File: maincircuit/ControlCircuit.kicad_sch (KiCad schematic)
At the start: 4 parts, among them J1 Conn_01x14_Socket, J2 Conn_01x14_Socket, J3 Conn_01x02_Pin, J4 Conn_01x02_Pin

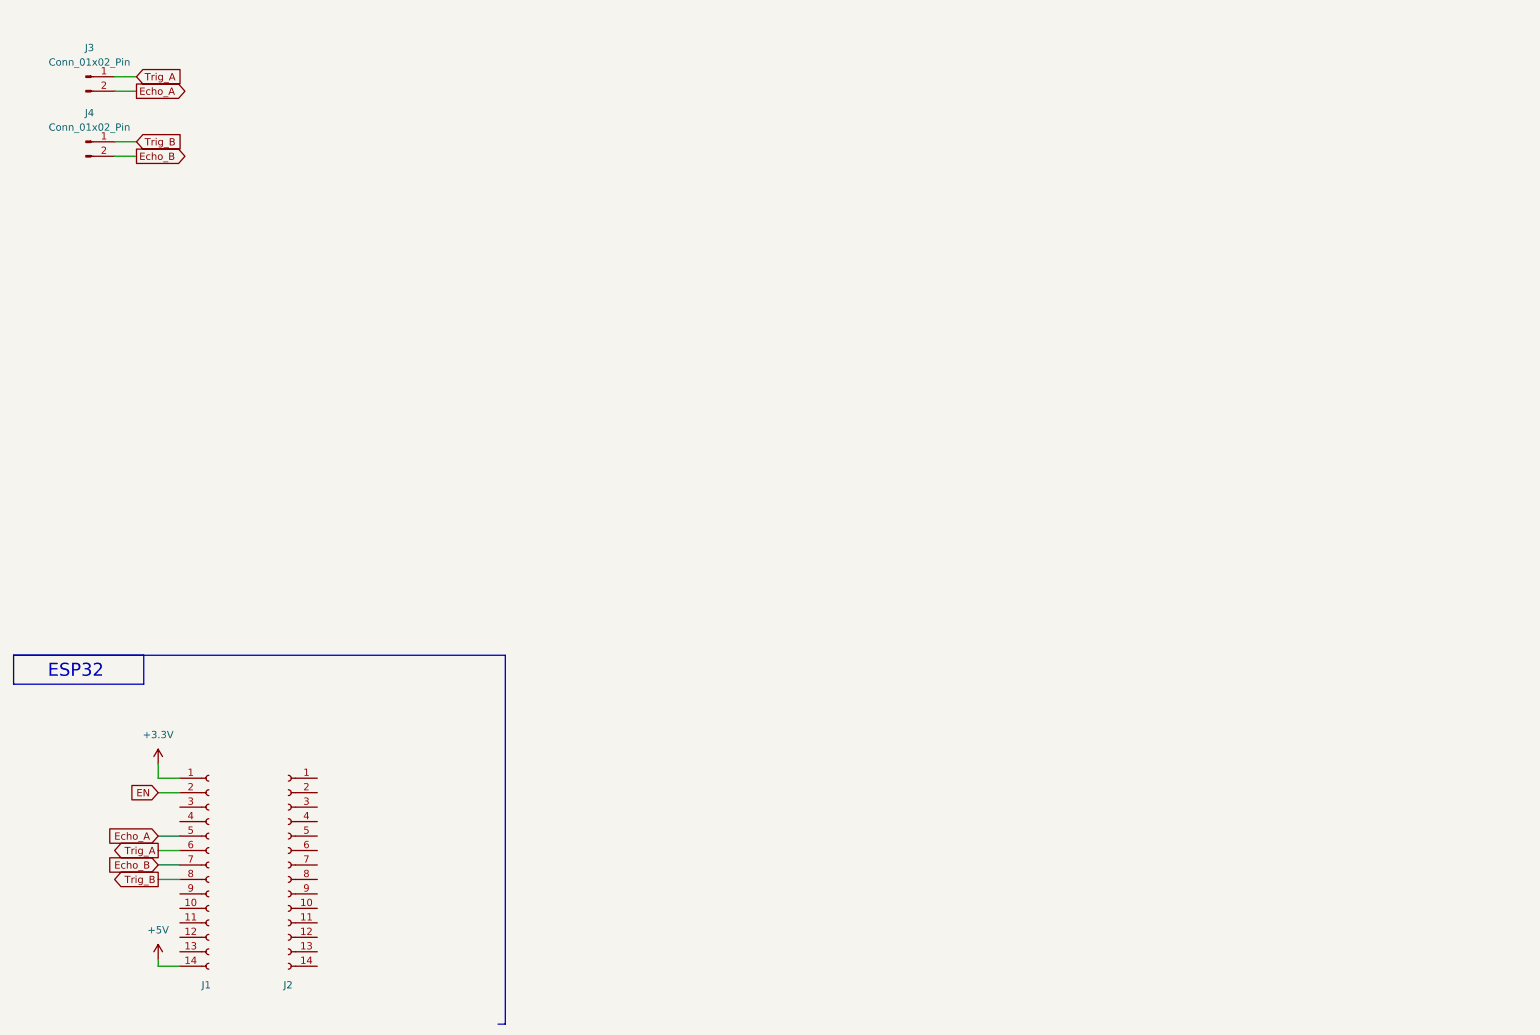
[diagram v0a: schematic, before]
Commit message: add: 07/13進捗分(主にcontrol回路)
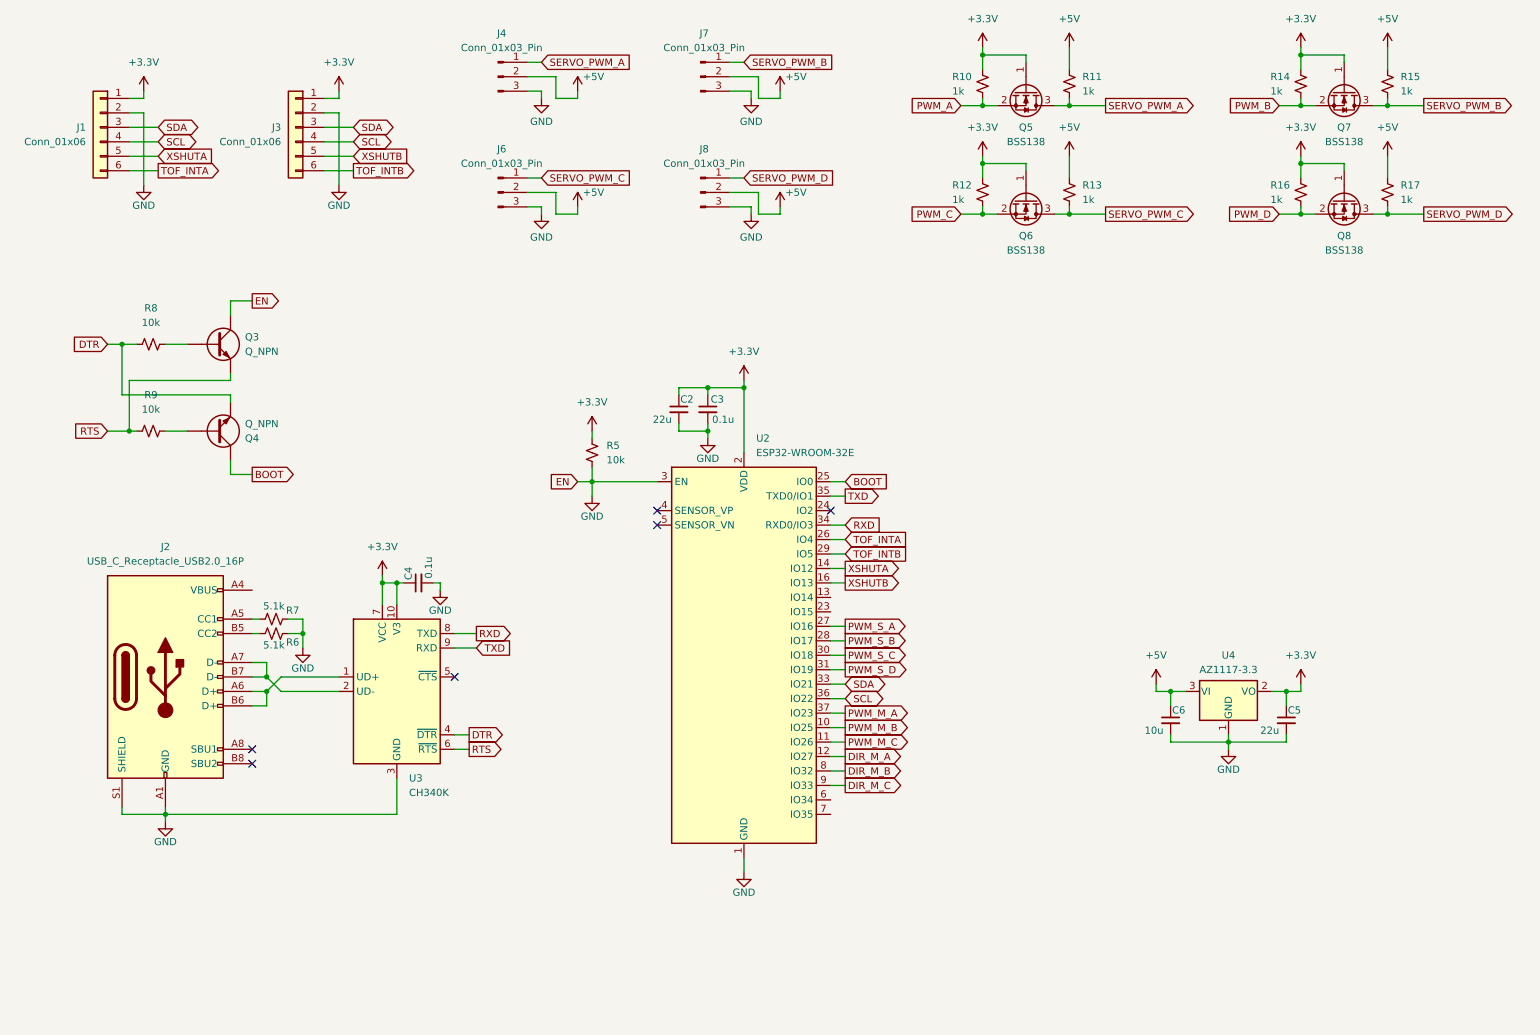
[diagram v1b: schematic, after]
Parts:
- removed J1, J2: Conn_01x14_Socket, symbol Connector:Conn_01x14_Socket
- removed J3, J4: Conn_01x02_Pin, symbol Connector:Conn_01x02_Pin
- added C2, C5: 22u, Capacitor_SMD:C_0603_1608Metric_Pad1.08x0.95mm_HandSolder, symbol Device:C_Small
- added C3, C4: 0.1u, Capacitor_SMD:C_0603_1608Metric_Pad1.08x0.95mm_HandSolder, symbol Device:C_Small
- added C6: 10u, Capacitor_SMD:C_0603_1608Metric_Pad1.08x0.95mm_HandSolder, symbol Device:C_Small
- added J1, J3: Conn_01x06, Connector_JST:JST_ZH_B6B-ZR_1x06_P1.50mm_Vertical, symbol Connector_Generic:Conn_01x06
- added J2: USB_C_Receptacle_USB2.0_16P, symbol Connector:USB_C_Receptacle_USB2.0_16P
- added J4, J6, J7, J8: Conn_01x03_Pin, symbol Connector:Conn_01x03_Pin
- added Q3, Q4: Q_NPN, Package_TO_SOT_SMD:SOT-23, symbol Device:Q_NPN
- added Q5, Q6, Q7, Q8: BSS138, Package_TO_SOT_SMD:SOT-23, symbol Transistor_FET:BSS138
- added R10, R11, R12, R13, R14, R15, R16, R17: 1k, symbol Device:R_Small_US
- added R5, R8, R9: 10k, symbol Device:R_Small_US
- added R6, R7: 5.1k, symbol Device:R_Small_US
- added U2: ESP32-WROOM-32E, RF_Module:ESP32-WROOM-32D, symbol RF_Module:ESP32-WROOM-32E
- added U3: CH340K, Package_SO:SSOP-10-1EP_3.9x4.9mm_P1mm_EP2.1x3.3mm, symbol Interface_USB:CH340K
- added U4: AZ1117-3.3, Package_TO_SOT_SMD:SOT-223, symbol Regulator_Linear:AZ1117-3.3
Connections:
- net +3.3V: now also C2.1, C3.1, C4.1, C5.1, J1.1 (Pin_1), J3.1 (Pin_1), Q5.1 (G), Q6.1 (G), Q7.1 (G), Q8.1 (G), R10.1, R12.1, R14.1, R16.1, R5.1, U2.2 (VDD), U3.10 (V3), U3.7 (VCC), U4.2 (VO)
- net +5V: now also C6.1, J4.2 (Pin_2), J6.2 (Pin_2), J7.2 (Pin_2), J8.2 (Pin_2), R11.1, R13.1, R15.1, R17.1, U4.3 (VI)
- new net: Q4.B, R9.2
- new net: J2.A5 (CC1), R7.1
- new net: Q3.B, R8.2
- new net: J2.A6 (D+), J2.B6 (D+), U3.1 (UD+)
- new net: J2.A7 (D-), J2.B7 (D-), U3.2 (UD-)
- new net: J2.B5 (CC2), R6.1
- new net: J2.A4 (VBUS), J2.A9 (VBUS), J2.B4 (VBUS), J2.B9 (VBUS)
- new net BOOT: Q4.C, U2.25 (IO0)
- new net DIR_M_A: U2.12 (IO27)
- new net DIR_M_B: U2.8 (IO32)
- new net DIR_M_C: U2.9 (IO33)
- new net DTR: Q4.E, R8.1, U3.4 (~{DTR})
- new net GND: C2.2, C3.2, C4.2, C5.2, C6.2, J1.2 (Pin_2), J2.A1 (GND), J2.A12 (GND), J2.B1 (GND), J2.B12 (GND), J2.S1 (SHIELD), J3.2 (Pin_2), J4.3 (Pin_3), J6.3 (Pin_3), J7.3 (Pin_3), J8.3 (Pin_3), Q3.C, R5.2, R6.2, R7.2, U2.1 (GND), U2.15 (GND), U2.3 (EN), U2.38 (GND), U2.39 (GND), U3.11 (GND), U3.3 (GND), U4.1 (GND)
- new net PWM_A: Q5.2 (S), R10.2
- new net PWM_B: Q7.2 (S), R14.2
- new net PWM_C: Q6.2 (S), R12.2
- new net PWM_D: Q8.2 (S), R16.2
- new net PWM_M_A: U2.37 (IO23)
- new net PWM_M_B: U2.10 (IO25)
- new net PWM_M_C: U2.11 (IO26)
- new net PWM_S_A: U2.27 (IO16)
- new net PWM_S_B: U2.28 (IO17)
- new net PWM_S_C: U2.30 (IO18)
- new net PWM_S_D: U2.31 (IO19)
- new net RTS: Q3.E, R9.1, U3.6 (~{RTS})
- new net RXD: U2.34 (RXD0/IO3), U3.8 (TXD)
- new net SCL: J1.4 (Pin_4), J3.4 (Pin_4), U2.36 (IO22)
- new net SDA: J1.3 (Pin_3), J3.3 (Pin_3), U2.33 (IO21)
- new net SERVO_PWM_A: J4.1 (Pin_1), Q5.3 (D), R11.2
- new net SERVO_PWM_B: J7.1 (Pin_1), Q7.3 (D), R15.2
- new net SERVO_PWM_C: J6.1 (Pin_1), Q6.3 (D), R13.2
- new net SERVO_PWM_D: J8.1 (Pin_1), Q8.3 (D), R17.2
- new net TOF_INTA: J1.6 (Pin_6), U2.26 (IO4)
- new net TOF_INTB: J3.6 (Pin_6), U2.29 (IO5)
- new net TXD: U2.35 (TXD0/IO1), U3.9 (RXD)
- new net XSHUTA: J1.5 (Pin_5), U2.14 (IO12)
- new net XSHUTB: J3.5 (Pin_5), U2.16 (IO13)
- no-connect marks 0 -> 6
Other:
- note removed: "ESP32"

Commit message: [add]ControlCircuit完成
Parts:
- removed J4, J6, J7, J8: Conn_01x03_Pin, symbol Connector:Conn_01x03_Pin
- added C10, C3: 0.1u, Capacitor_SMD:C_0603_1608Metric_Pad1.08x0.95mm_HandSolder, symbol Device:C_Small
- added C5: 10u, Capacitor_SMD:C_0603_1608Metric_Pad1.08x0.95mm_HandSolder, symbol Device:C_Small
- added C6, C7: C_Small, Capacitor_SMD:C_0603_1608Metric_Pad1.08x0.95mm_HandSolder, symbol Device:C_Small
- added C8, C9: 22u, Capacitor_SMD:C_0603_1608Metric_Pad1.08x0.95mm_HandSolder, symbol Device:C_Small
- added D1: D_Small, Diode_SMD:Vishay_SMPA, symbol Device:D_Small
- added D10, D11, D12, D13, D14, D15, D4, D5, D6, D7, D8, D9: LED, LED_SMD:LED_0603_1608Metric, symbol Device:LED
- added D2, D3: D_Schottky_Small, Diode_SMD:Nexperia_CFP3_SOD-123W, symbol Device:D_Schottky_Small
- added FB1, FB2: FerriteBead_Small, Inductor_SMD:L_0603_1608Metric_Pad1.05x0.95mm_HandSolder, symbol Device:FerriteBead_Small
- added H1, H2, H3, H4: MountingHole, MountingHole:MountingHole_3.2mm_M3, symbol Mechanical:MountingHole
- added J10, J11: Conn_02x03_Odd_Even, Connector_PinHeader_2.54mm:PinHeader_2x03_P2.54mm_Horizontal, symbol Connector_Generic:Conn_02x03_Odd_Even
- added J12: Conn_02x04_Odd_Even, Connector_PinHeader_2.54mm:PinHeader_2x04_P2.54mm_Horizontal, symbol Connector_Generic:Conn_02x04_Odd_Even
- added J13: Conn_01x03_Pin, Connector_PinHeader_2.54mm:PinHeader_1x03_P2.54mm_Horizontal, symbol Connector:Conn_01x03_Pin
- added J14: Conn_01x02_Pin, Connector_PinHeader_2.54mm:PinHeader_1x02_P2.54mm_Vertical, symbol Connector:Conn_01x02_Pin
- added J15: Conn_01x05_Pin, Connector_PinHeader_2.54mm:PinHeader_1x05_P2.54mm_Horizontal, symbol Connector:Conn_01x05_Pin
- added J16: Conn_01x02_Pin, Connector_PinHeader_2.54mm:PinHeader_1x02_P2.54mm_Horizontal, symbol Connector:Conn_01x02_Pin
- added J3: Conn_02x02_Counter_Clockwise, Connector_PinSocket_2.54mm:PinSocket_2x02_P2.54mm_Vertical, symbol Connector_Generic:Conn_02x02_Counter_Clockwise
- added J5: Conn_02x04_Counter_Clockwise, Connector_PinHeader_2.54mm:PinHeader_2x04_P2.54mm_Vertical, symbol Connector_Generic:Conn_02x04_Counter_Clockwise
- added J6: Conn_02x04_Counter_Clockwise, Connector_PinSocket_2.54mm:PinSocket_2x04_P2.54mm_Vertical, symbol Connector_Generic:Conn_02x04_Counter_Clockwise
- added J7, J8, J9: Conn_01x03, Connector_JST:JST_XH_S3B-XH-A_1x03_P2.50mm_Horizontal, symbol Connector_Generic:Conn_01x03
- added R10, R9: 2.2k, Resistor_SMD:R_0603_1608Metric_Pad0.98x0.95mm_HandSolder, symbol Device:R_Small_US
- added R11, R12, R6, R7, R8: 0, Resistor_SMD:R_0603_1608Metric_Pad0.98x0.95mm_HandSolder, symbol Device:R_Small_US
- added R13: 100k, Resistor_SMD:R_0603_1608Metric_Pad0.98x0.95mm_HandSolder, symbol Device:R_Small_US
- added R18: 3.3k, Resistor_SMD:R_0603_1608Metric_Pad0.98x0.95mm_HandSolder, symbol Device:R_Small_US
- added R19, R20, R21, R22, R23, R24, R25, R26, R27, R28, R29: 1k, Resistor_SMD:R_0603_1608Metric_Pad0.98x0.95mm_HandSolder, symbol Device:R_Small_US
- added U3: NJM7805SDL1, Package_TO_SOT_SMD:TO-252-2, symbol Library:NJM7805SDL1
- added U4: STM32C011F4Px, Package_SO:TSSOP-20_4.4x6.5mm_P0.65mm, symbol MCU_ST_STM32C0:STM32C011F4Px
- added Y1: Crystal_Small, Crystal:Crystal_SMD_3215-2Pin_3.2x1.5mm, symbol Device:Crystal_Small
- J1: renamed from J2; footprint (none) -> Library:5077CR-16-SMC2-BK-TR
- R1: renamed from R8; footprint (none) -> Resistor_SMD:R_0603_1608Metric_Pad0.98x0.95mm_HandSolder
- R14: renamed from R10; footprint (none) -> Resistor_SMD:R_0603_1608Metric_Pad0.98x0.95mm_HandSolder
- R15: renamed from R12; footprint (none) -> Resistor_SMD:R_0603_1608Metric_Pad0.98x0.95mm_HandSolder
- R16: renamed from R11; footprint (none) -> Resistor_SMD:R_0603_1608Metric_Pad0.98x0.95mm_HandSolder
- R17: renamed from R13; footprint (none) -> Resistor_SMD:R_0603_1608Metric_Pad0.98x0.95mm_HandSolder
- R2: renamed from R9; footprint (none) -> Resistor_SMD:R_0603_1608Metric_Pad0.98x0.95mm_HandSolder
- R3: renamed from R7; footprint (none) -> Resistor_SMD:R_0603_1608Metric_Pad0.98x0.95mm_HandSolder
- R30: renamed from R14; footprint (none) -> Resistor_SMD:R_0603_1608Metric_Pad0.98x0.95mm_HandSolder
- R31: renamed from R16; footprint (none) -> Resistor_SMD:R_0603_1608Metric_Pad0.98x0.95mm_HandSolder
- R32: renamed from R15; footprint (none) -> Resistor_SMD:R_0603_1608Metric_Pad0.98x0.95mm_HandSolder
- R33: renamed from R17; footprint (none) -> Resistor_SMD:R_0603_1608Metric_Pad0.98x0.95mm_HandSolder
- R4: renamed from R6; footprint (none) -> Resistor_SMD:R_0603_1608Metric_Pad0.98x0.95mm_HandSolder
- R5: value 10k -> 0; footprint (none) -> Resistor_SMD:R_0603_1608Metric_Pad0.98x0.95mm_HandSolder
- renumbered C2 to C1, C6 to C11, C5 to C12, C4 to C2, C3 to C4, J1 to J2, J3 to J4, Q3 to Q1, Q4 to Q2, Q5 to Q3, Q6 to Q4, Q7 to Q5, Q8 to Q6, U3 to U1, U4 to U5
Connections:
- net PWM_A is gone; now on net PWM_S_A: Q3.2 (S), R14.2
- net PWM_B is gone; now on net PWM_S_B: Q5.2 (S), R30.2
- net PWM_C is gone; now on net PWM_S_C: Q4.2 (S), R15.2
- net PWM_D is gone; now on net PWM_S_D: Q6.2 (S), R31.2
- net +3.3V: now also U5.4 (VO2), C3.1, D3.2 (A), FB1.2, FB2.2, J15.1 (Pin_1), J16.1 (Pin_1), R10.1, R22.1, R9.1; no longer C1.1, C4.1, R5.1, U2.2 (VDD)
- net +5V: now also D3.1 (K), J10.3 (Pin_3), J10.4 (Pin_4), J11.3 (Pin_3), J11.4 (Pin_4), J13.2 (Pin_2), R21.1
- net DIR_M_A: now also U2.26 (IO4), J7.1 (Pin_1); no longer U2.12 (IO27)
- net DIR_M_B: now also U2.28 (IO17), J8.1 (Pin_1); no longer U2.8 (IO32)
- net DIR_M_C: now also U2.30 (IO18), J9.1 (Pin_1); no longer U2.9 (IO33)
- net DTR: now also Q2.2 (E); no longer Q2.E
- net GND: now also C10.2, C3.2, C5.2, C6.2, C7.2, C8.2, C9.2, D10.1 (K), D11.1 (K), D12.1 (K), D13.1 (K), D14.1 (K), D15.1 (K), D4.1 (K), D5.1 (K), D6.1 (K), D7.1 (K), D8.1 (K), D9.1 (K), J10.5 (Pin_5), J10.6 (Pin_6), J11.5 (Pin_5), J11.6 (Pin_6), J14.2 (Pin_2), J15.3 (Pin_3), J3.3 (Pin_3), J3.4 (Pin_4), J5.5 (Pin_5), J5.6 (Pin_6), J5.7 (Pin_7), J5.8 (Pin_8), J6.5 (Pin_5), J6.6 (Pin_6), J6.7 (Pin_7), J6.8 (Pin_8), J7.3 (Pin_3), J8.3 (Pin_3), J9.3 (Pin_3), R13.2, U3.2 (GND), U4.5 (VSS); no longer Q1.C, R5.2, U2.3 (EN)
- net PWM_M_A: now also U2.27 (IO16), J7.2 (Pin_2); no longer U2.37 (IO23)
- net PWM_M_B: now also U2.29 (IO5), J8.2 (Pin_2); no longer U2.10 (IO25)
- net PWM_M_C: now also U2.31 (IO19), J9.2 (Pin_2); no longer U2.11 (IO26)
- net PWM_S_A: now also U2.13 (IO14); no longer U2.27 (IO16)
- net PWM_S_B: now also U2.14 (IO12); no longer U2.28 (IO17)
- net PWM_S_C: now also U2.16 (IO13); no longer U2.30 (IO18)
- net PWM_S_D: now also U2.23 (IO15); no longer U2.31 (IO19)
- net RTS: now also Q1.2 (E); no longer Q1.E
- net RXD: now also R5.2; no longer U1.8 (TXD)
- net SCL: now also J3.2 (Pin_2), R10.2, R11.1, R8.2; no longer U2.36 (IO22)
- net SDA: now also J3.1 (Pin_1), R12.1, R7.2, R9.2; no longer U2.33 (IO21)
- net SERVO_PWM_A: now also J10.1 (Pin_1)
- net SERVO_PWM_B: now also J10.2 (Pin_2)
- net SERVO_PWM_C: now also J11.1 (Pin_1)
- net SERVO_PWM_D: now also J11.2 (Pin_2)
- net TOF_INTA: now also U2.10 (IO25); no longer U2.26 (IO4)
- net TOF_INTB: now also U2.12 (IO27); no longer U2.29 (IO5)
- net TXD: now also R6.2; no longer U1.9 (RXD)
- net XSHUTA: now also U2.9 (IO33); no longer U2.14 (IO12)
- net XSHUTB: now also U2.11 (IO26); no longer U2.16 (IO13)
- net at R2.2: now also Q2.1 (B); no longer Q2.B
- net LED3: now reaches U2.6 (IO34)
- net LED3: now also R25.1
- net EMERGENCY: now reaches U2.7 (IO35)
- net EMERGENCY: now also J14.1 (Pin_1), R26.1
- net at R1.2: now also Q1.1 (B); no longer Q1.B
- net UD+: now reaches J1.A6 (D+), J1.B6 (D+), U1.1 (UD+)
- net UD-: now reaches J1.A7 (D-), J1.B7 (D-), U1.2 (UD-)
- net +5VD: now reaches J1.A4 (VBUS), J1.A9 (VBUS), J1.B4 (VBUS), J1.B9 (VBUS)
- net +5VD: now also J13.3 (Pin_3), R20.1
- net BOOT renamed BOOT_ESP
- net BOOT_ESP: now also Q2.3 (C); no longer Q2.C
- new net: D8.2 (A), R22.2
- new net: D4.2 (A), R18.2
- new net: R12.2, U4.1 (PB7)
- new net: C6.1, U4.2 (PC14), Y1.2
- new net: R11.2, U4.20 (PB6)
- new net: C7.1, U4.3 (PC15), Y1.1
- new net: C10.1, C9.1, FB2.1, U4.4 (VDD)
- new net: D11.2 (A), R25.2
- new net: R7.1, U2.33 (IO21)
- new net: C1.1, C4.1, FB1.1, U2.2 (VDD)
- new net: R8.1, U2.36 (IO22)
- new net: D12.2 (A), R26.2
- new net: D1.2 (A), J5.1 (Pin_1), J5.2 (Pin_2), J5.3 (Pin_3), J5.4 (Pin_4), J6.1 (Pin_1), J6.2 (Pin_2), J6.3 (Pin_3), J6.4 (Pin_4)
- new net: D15.2 (A), R29.2
- new net: D14.2 (A), R28.2
- new net: R6.1, U1.9 (RXD)
- new net: D10.2 (A), R24.2
- new net: D7.2 (A), R21.2
- new net: R5.1, U1.8 (TXD)
- new net: D9.2 (A), R23.2
- new net: D6.2 (A), R20.2
- new net: D13.2 (A), R27.2
- new net: D5.2 (A), R19.2
- new net +5VP: C8.1, D2.2 (A), J13.1 (Pin_1), R19.1, U3.3 (VO)
- new net +BATT: C5.1, D1.1 (K), D2.1 (K), R18.1, U3.1 (VI)
- new net EN: Q1.3 (C), U2.3 (EN)
- new net LED1: R23.1, U2.37 (IO23)
- new net LED2: R24.1, U2.8 (IO32)
- new net LED4: R27.1, U4.15 (PA8)
- new net LED5: R28.1, U4.16 (PA9/PA11)
- new net LED6: R29.1, U4.17 (PA10/PA12)
- new net NRST: J15.5 (Pin_5), U4.6 (PF2)
- new net STP_M1_A: J12.1 (Pin_1), U4.7 (PA0)
- new net STP_M1_B: J12.3 (Pin_3), U4.8 (PA1)
- new net STP_M1_C: J12.5 (Pin_5), U4.9 (PA2)
- new net STP_M1_D: J12.7 (Pin_7), U4.10 (PA3)
- new net STP_M2_A: J12.2 (Pin_2), U4.11 (PA4)
- new net STP_M2_B: J12.4 (Pin_4), U4.12 (PA5)
- new net STP_M2_C: J12.6 (Pin_6), U4.13 (PA6)
- new net STP_M2_D: J12.8 (Pin_8), U4.14 (PA7)
- new net SWCLK: J15.2 (Pin_2), J16.2 (Pin_2), R13.1, U4.19 (PA14)
- new net SWDIO: J15.4 (Pin_4), U4.18 (PA13)
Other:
- note added: "Connector"
- note added: "LED"
- note added: "Level Shifter"
- note added: "MCU"
- note added: "Option"
- note added: "Regulator"
- note added: "USB"
- moved on the sheet: C1, C11, C12, C2, C4, J1, J2, J4, Q1, Q2, Q3, Q4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
